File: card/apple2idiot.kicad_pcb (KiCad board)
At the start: 2 copper layers, 167.6 x 77.5 mm, 5 parts, among them J1 CARD EDGE, J2 HEADER BLOCK, U1 IDT7132, U2 ESP32-WROOM-32

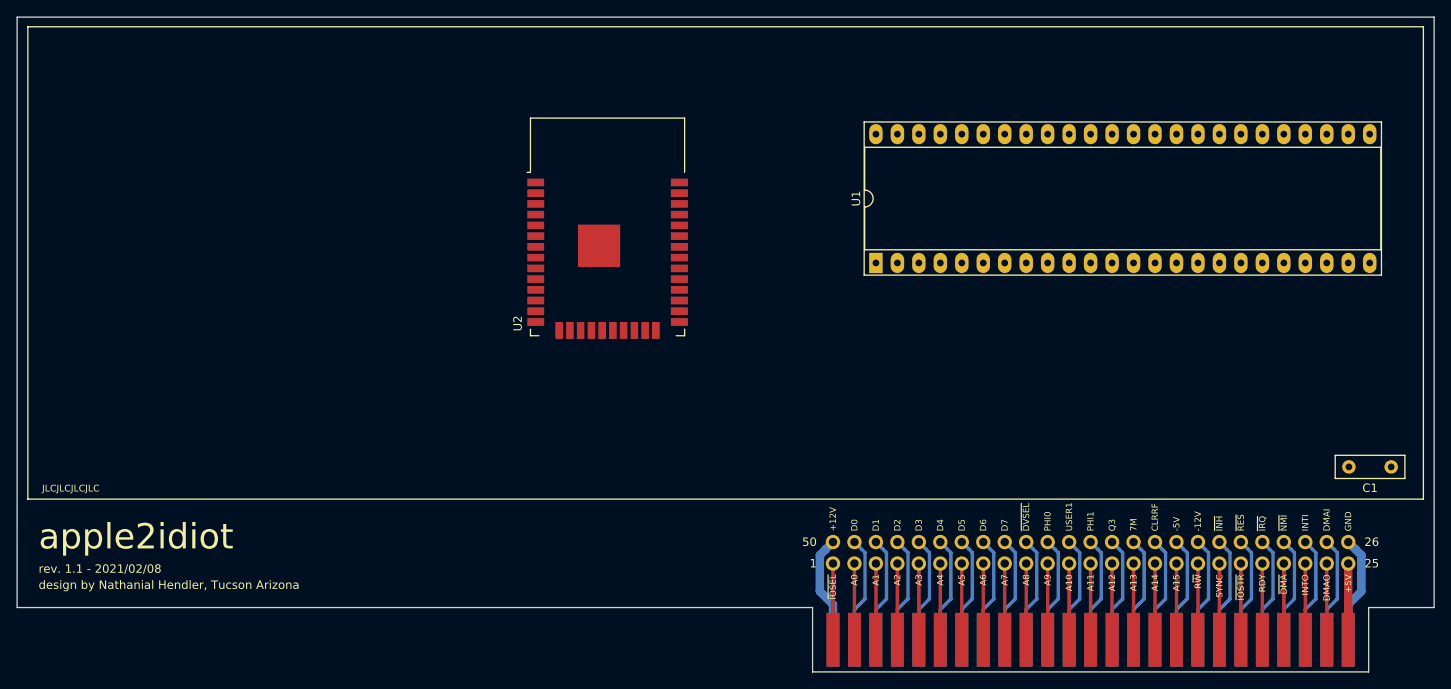
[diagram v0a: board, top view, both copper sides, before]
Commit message: ESP w/ webserver writes to RAM
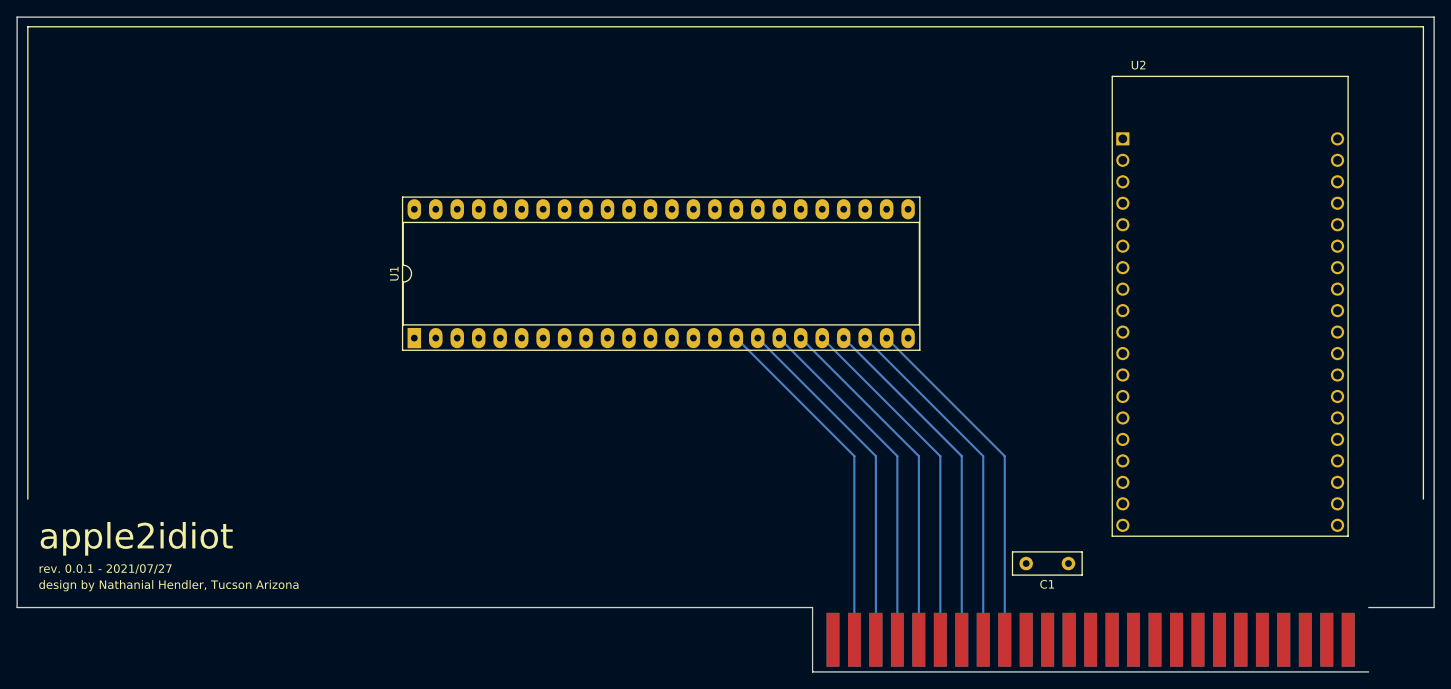
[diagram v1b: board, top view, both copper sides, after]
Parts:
- removed J2: HEADER BLOCK, pub:PinSocket_2x25_P2.54mm_Vertical_CCW_Mirrored_NoSilk
- U2: value ESP32-WROOM-32 -> ESP32-DEVKITC-32D; footprint RF_Module:ESP32-WROOM-32 -> ESPDEVKIT:MODULE_ESP32-DEVKITC-32D
- moved U2 73.9 mm to (217.2, 88.9)
- moved U1 55.3 mm to (120.7, 92.7)
- moved C1 39.9 mm to (198.0, 119.4)
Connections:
- U1 pad 25: /D7R -> Net-(U1-Pad25)
- U1 pad 26: /D6R -> Net-(U1-Pad26)
- U1 pad 27: /D5R -> Net-(U1-Pad27)
- U1 pad 28: /D4R -> Net-(U1-Pad28)
- U1 pad 29: /D3R -> Net-(U1-Pad29)
- U1 pad 30: /D2R -> Net-(U1-Pad30)
- U1 pad 31: /D1R -> Net-(U1-Pad31)
- U1 pad 32: /D0R -> Net-(U1-Pad32)
- U1 pad 48: VCC -> +5V
- U2 pad 1: GND -> Net-(U2-Pad1)
- U2 pad 10: Net-(U1-Pad41) -> Net-(U1-Pad40)
- U2 pad 11: Net-(U1-Pad40) -> Net-(U1-Pad39)
- U2 pad 12: Net-(U1-Pad39) -> Net-(U1-Pad27)
- U2 pad 13: Net-(U2-Pad13) -> Net-(U1-Pad25)
- U2 pad 14: Net-(U2-Pad14) -> GND
- U2 pad 15: GND -> Net-(U1-Pad26)
- U2 pad 19: Net-(U2-Pad19) -> +5V
- U2 pad 20: Net-(U2-Pad20) -> GND
- U2 pad 21: Net-(U2-Pad21) -> Net-(U1-Pad42)
- U2 pad 22: Net-(U2-Pad22) -> Net-(U1-Pad32)
- U2 pad 25: Net-(U2-Pad25) -> Net-(U1-Pad31)
- U2 pad 26: Net-(U1-Pad38) -> GND
- U2 pad 27: Net-(U2-Pad27) -> Net-(U1-Pad30)
- U2 pad 28: Net-(U2-Pad28) -> Net-(U1-Pad29)
- U2 pad 35: Net-(U2-Pad35) -> Net-(U1-Pad28)
- U2 pad 37: Net-(U1-Pad42) -> Net-(U2-Pad37)
- U2 pad 38: GND -> Net-(U2-Pad38)
- U2 pad 5: Net-(U2-Pad5) -> /~IOSEL
- U2 pad 6: Net-(U1-Pad45) -> Net-(U1-Pad3)
- U2 pad 7: Net-(U1-Pad3) -> Net-(U1-Pad38)
- U2 pad 8: Net-(U2-Pad8) -> Net-(U1-Pad37)
- U2 pad 9: /~IOSEL -> Net-(U1-Pad41)
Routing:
- net /D7: track 12.6 -> 41.5 mm
- net /D4: track 12.6 -> 41.5 mm
- net /D3: track 12.6 -> 41.5 mm
- net /D2: track 12.6 -> 41.5 mm
- net /D1: track 12.6 -> 41.5 mm
- net /D0: track 12.6 -> 41.5 mm
- net /D6: track 12.6 -> 41.5 mm
- net /D5: track 12.6 -> 41.5 mm
- net /GND: track 12.8 -> 0.00 mm
- net /+12V: track 12.8 -> 0.00 mm
- net /-5V: track 12.6 -> 0.00 mm
- net /~RES: track 12.6 -> 0.00 mm
- net /~NMI: track 12.6 -> 0.00 mm
- net /~IRQ: track 12.6 -> 0.00 mm
- net /~INH: track 12.6 -> 0.00 mm
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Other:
- board text added: "rev. 0.0.1 - 2021/07/27"
- board text removed: "+12V"
- board text removed: "+5V"
- board text removed: "-12V"
- board text removed: "-5V"
- board text removed: "1"
- board text removed: "25"
- board text removed: "26"
- board text removed: "50"
- board text removed: "7M"
- board text removed: "A0"
- board text removed: "A1"
- board text removed: "A10"
- board text removed: "A11"
- board text removed: "A12"
- board text removed: "A13"
- board text removed: "A14"
- board text removed: "A15"
- board text removed: "A2"
- board text removed: "A3"
- board text removed: "A4"
- board text removed: "A5"
- board text removed: "A6"
- board text removed: "A7"
- board text removed: "A8"
- board text removed: "A9"
- board text removed: "CLRRF"
- board text removed: "D0"
- board text removed: "D1"
- board text removed: "D2"
- board text removed: "D3"
- board text removed: "D4"
- board text removed: "D5"
- board text removed: "D6"
- board text removed: "D7"
- board text removed: "DMAI"
- board text removed: "DMAO"
- board text removed: "GND"
- board text removed: "INTI"
- board text removed: "INTO"
- board text removed: "JLCJLCJLCJLC"
- board text removed: "PHI0"
- board text removed: "PHI1"
- board text removed: "Q3"
- board text removed: "RDY"
- board text removed: "R~W"
- board text removed: "SYNC"
- board text removed: "USER1"
- board text removed: "rev. 1.1 - 2021/02/08"
- board text removed: "~DMA"
- board text removed: "~DVSEL"
- board text removed: "~INH"
- board text removed: "~IOSEL"
- board text removed: "~IOSTR"
- board text removed: "~IRQ"
- board text removed: "~NMI"
- board text removed: "~RES"

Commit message: going to silver city
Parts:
- moved U1 11.8 mm to (131.5, 97.2)
- moved C1 6.49 mm to (204.5, 120.0)
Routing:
- net GND: track 0.00 -> 290.0 mm, vias 0 -> 2
- net Net-(U1-Pad28): track 0.00 -> 216.4 mm
- net +5V: track 0.00 -> 186.2 mm
- net Net-(U1-Pad29): track 0.00 -> 182.7 mm
- net Net-(U1-Pad30): track 0.00 -> 172.5 mm
- net Net-(U1-Pad31): track 0.00 -> 159.2 mm
- net /R~W: track 0.00 -> 153.6 mm
- net Net-(U1-Pad46): track 0.00 -> 141.5 mm
- net Net-(U1-Pad3): track 0.00 -> 121.3 mm
- net /~IOSEL: track 0.00 -> 111.8 mm
- net /~DEVSEL: track 0.00 -> 93.4 mm
- net Net-(U1-Pad42): track 0.00 -> 87.4 mm
- net Net-(U1-Pad38): track 0.00 -> 84.6 mm
- net Net-(U1-Pad37): track 0.00 -> 84.0 mm
- net Net-(U1-Pad41): track 0.00 -> 68.6 mm
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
